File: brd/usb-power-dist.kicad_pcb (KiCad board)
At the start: 2 copper layers, 50 x 50 mm, 40 parts, among them J1 POWER IN, J2 USB_A, J3 USB_A, J4 CASC IN, J5 CASC OUT, U1 TPS2552D, U2 TPS2552D, U3 TPS2513

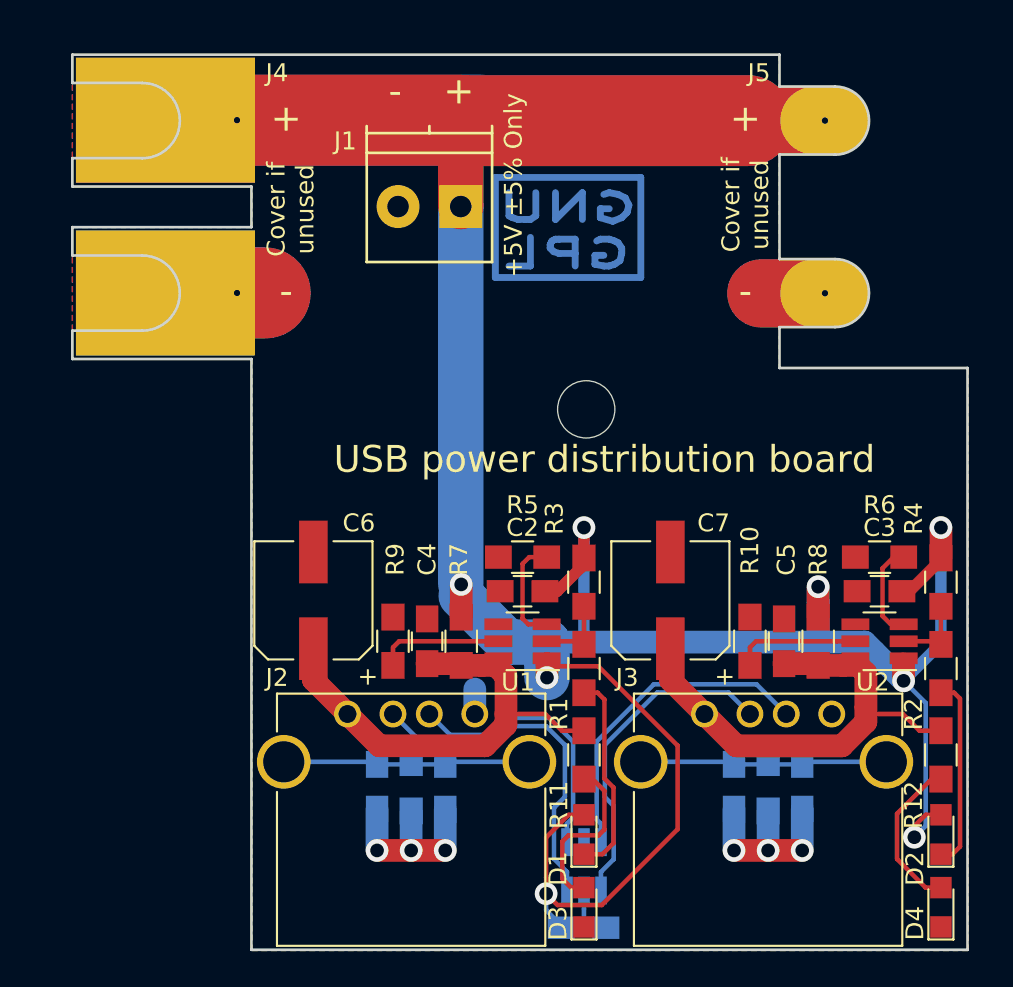
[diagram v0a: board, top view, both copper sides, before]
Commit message: recolocados componentes por fallo en asignacion de pines en TPS2552, modificada posicion de serigrafias, añadida serigrafia de version y tabla de corriente, cambiado footprint de conector de entrada y alargados conectores de borde de placa de cascada machos
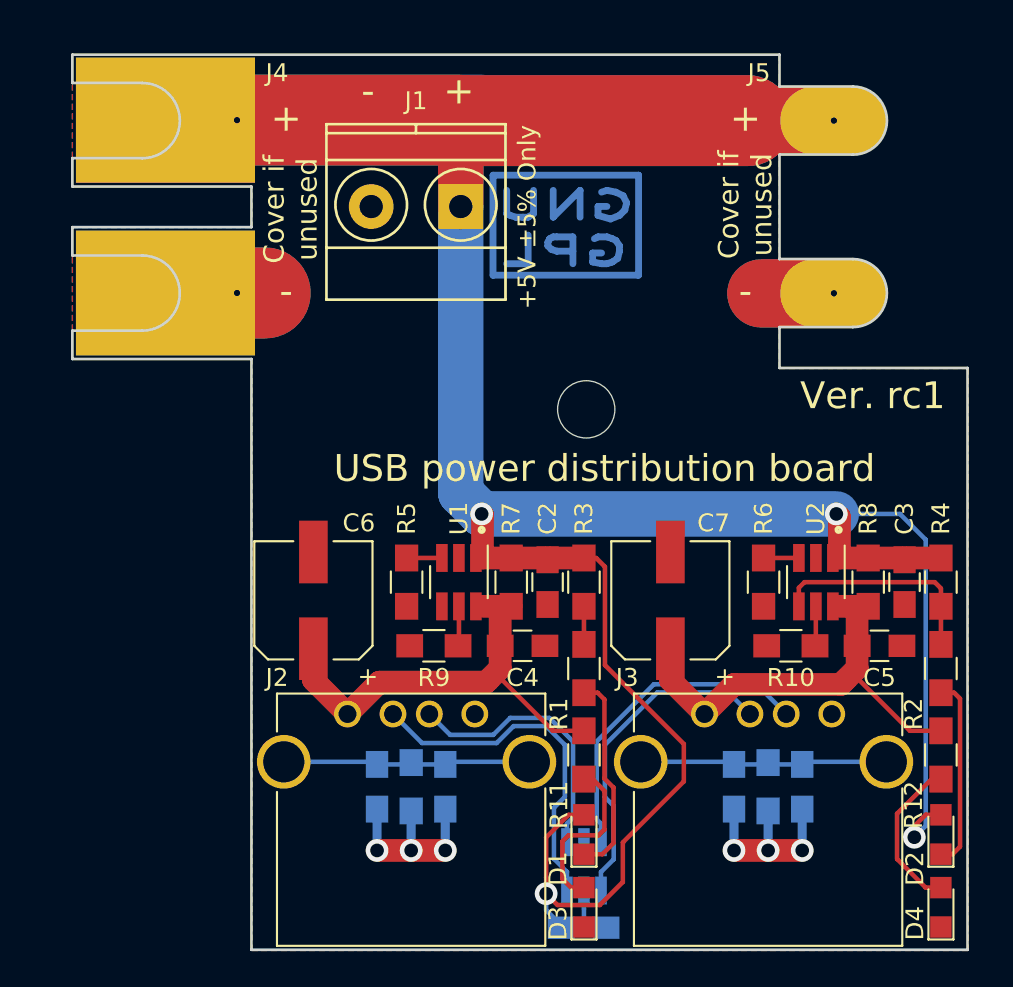
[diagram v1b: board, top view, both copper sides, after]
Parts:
- J1: footprint Terminal_Blocks:TerminalBlock_Pheonix_PT-3.5mm_2pol -> Terminal_Blocks:TerminalBlock_Pheonix_MKDS1.5-2pol
- moved R5 6.63 mm to (141.6, 110.5), turned to 270 degrees
- moved R6 6.63 mm to (161.5, 110.5), turned to 270 degrees
- moved C4 5.34 mm to (148.1, 114.0), turned to 0 degrees
- moved C5 5.34 mm to (168.0, 114.0), turned to 0 degrees
- moved U1 4.85 mm to (144.5, 110.5), turned to 270 degrees
- moved U2 4.85 mm to (164.5, 110.5), turned to 270 degrees
- moved R7 4.33 mm to (147.4, 110.5)
- moved R8 4.33 mm to (167.4, 110.5)
- moved R10 2.30 mm to (163.1, 114.0), turned to 180 degrees
- moved R9 2.30 mm to (143.1, 114.0), turned to 180 degrees
- moved C2 1.49 mm to (149.5, 110.5), turned to 270 degrees
- moved C3 1.49 mm to (169.4, 110.5), turned to 270 degrees
- moved REF** 0.18 mm to (150.5, 90.8)
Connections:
- U1 pad 2: Net-(R1-Pad1) -> GND
- U1 pad 4: GND -> Net-(R1-Pad1)
- U2 pad 2: Net-(R2-Pad1) -> GND
- U2 pad 4: GND -> Net-(R2-Pad1)
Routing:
- net +5V: track 205.9 -> 193.4 mm, vias 8 -> 4
- net Net-(R2-Pad1): track 4.28 -> 12.6 mm
- net Net-(R9-Pad1): track 7.04 -> 2.23 mm
- net Net-(R10-Pad1): track 7.04 -> 2.23 mm
- net Net-(R5-Pad1): track 6.05 -> 1.97 mm
- net Net-(R6-Pad1): track 5.48 -> 1.97 mm
- net Net-(C5-Pad1): track 28.1 -> 25.7 mm
- net Net-(R1-Pad1): track 4.28 -> 2.13 mm
- net Net-(C4-Pad1): track 27.8 -> 25.7 mm
- net GND: track 32.9 -> 33.5 mm
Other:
- outline, holes or cut-outs redrawn
- board text added: "Current R9/R10 100mA 226k 500mA 52k3 900mA 28k7 1500mA 16k9 No lim See doc"
- board text added: "Ver. rc1"
- board text removed: "[X] Comprobar footprints de conectores [X] Ubicación de montaje [X] Verificar forma de placa [X] Trazado completo [X] Colocar serigrafia [X] Añadir textos, polaridad y logos"

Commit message: corregido fallo ausencia de pista pin ¬FAULT
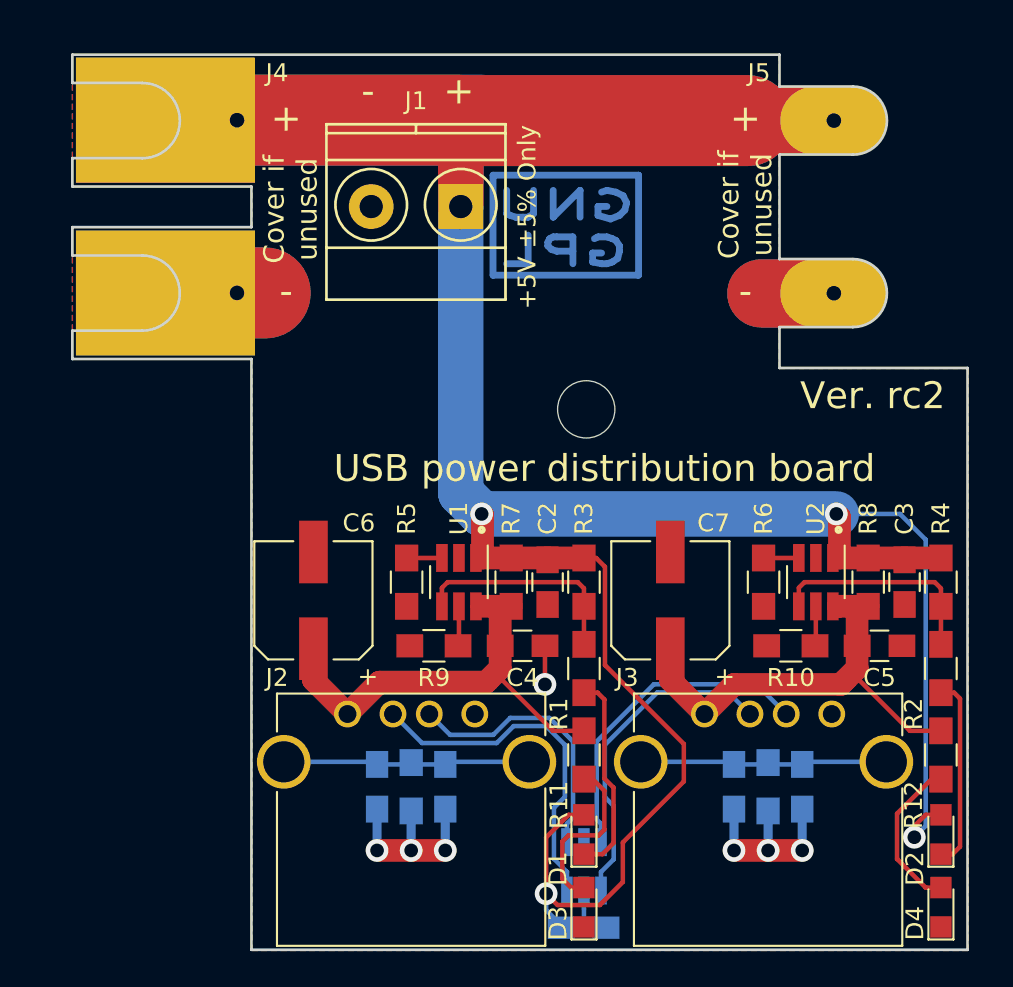
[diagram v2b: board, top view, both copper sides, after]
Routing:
- net Net-(R1-Pad1): track 2.13 -> 12.4 mm
- net GND: track 33.5 -> 36.0 mm, vias 6 -> 7
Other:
- board text added: "Ver. rc2"
- board text removed: "Ver. rc1"
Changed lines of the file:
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@@
   (general
     (links 74)
-    (no_connects 6)
-    (area 122.860999 80.950999 173.011001 131.101001)
+    (no_connects 5)
+    (area 101.330001 62.705 205.957143 139.733001)
     (thickness 1.6)
     (drawings 77)
-    (tracks 196)
+    (tracks 203)
     (zones 0)
     (modules 40)
@@
     (mod_text_size 1 1)
     (mod_text_width 0.15)
-    (pad_size 3.8 6)
-    (pad_drill 0.35)
+    (pad_size 7 10)
+    (pad_drill 0.8128)
     (pad_to_mask_clearance 0.2)
     (aux_axis_origin 0 0)
@@
     (add_net "Net-(C5-Pad1)")
   )
-  (module Capacitors_SMD:C_0805_HandSoldering (layer F.Cu)
-    (at 149.479 110.49 270)
-    (descr "Capacitor SMD 0805, hand soldering")
-    (tags "capacitor 0805")
-    (attr smd)
-    (fp_text reference C2 (at -3.556 0 270) (layer F.SilkS)
-      (effects (font (size 1 1) (thickness 0.15)))
-    )
-    (fp_text value 100nF (at 0 3.556 270) (layer F.Fab) hide
-      (effects (font (size 1 1) (thickness 0.15)))
-    )
-    (fp_text user %R (at 0 3.556 270) (layer F.Fab) hide
-      (effects (font (size 1 1) (thickness 0.15)))
-    )
-    (fp_line (start -1 0.62) (end -1 -0.62) (layer F.Fab) (width 0.1))
-    (fp_line (start 1 0.62) (end -1 0.62) (layer F.Fab) (width 0.1))
-    (fp_line (start 1 -0.62) (end 1 0.62) (layer F.Fab) (width 0.1))
-    (fp_line (start -1 -0.62) (end 1 -0.62) (layer F.Fab) (width 0.1))
-    (fp_line (start 0.5 -0.85) (end -0.5 -0.85) (layer F.SilkS) (width 0.12))
-    (fp_line (start -0.5 0.85) (end 0.5 0.85) (layer F.SilkS) (width 0.12))
-    (fp_line (start -2.25 -0.88) (end 2.25 -0.88) (layer F.CrtYd) (width 0.05))
-    (fp_line (start -2.25 -0.88) (end -2.25 0.87) (layer F.CrtYd) (width 0.05))
-    (fp_line (start 2.25 0.87) (end 2.25 -0.88) (layer F.CrtYd) (width 0.05))
-    (fp_line (start 2.25 0.87) (end -2.25 0.87) (layer F.CrtYd) (width 0.05))
-    (pad 1 smd rect (at -1.25 0 270) (size 1.5 1.25) (layers F.Cu F.Paste F.Mask)
-      (net 1 +5V))
-    (pad 2 smd rect (at 1.25 0 270) (size 1.5 1.25) (layers F.Cu F.Paste F.Mask)
-      (net 2 GND))
-    (model Capacitors_SMD.3dshapes/C_0805.wrl
-      (at (xyz 0 0 0))
-      (scale (xyz 1 1 1))
-      (rotate (xyz 0 0 0))
-    )
-  )
   (module TO_SOT_Packages_SMD:SOT-23-6_Handsoldering (layer F.Cu)
     (at 144.526 110.49 270)
@@
       (net 19 "Net-(R9-Pad1)"))
     (model ${KISYS3DMOD}/TO_SOT_Packages_SMD.3dshapes/SOT-23-6.wrl
+      (at (xyz 0 0 0))
+      (scale (xyz 1 1 1))
+      (rotate (xyz 0 0 0))
+    )
+  )
+  (module Capacitors_SMD:C_0805_HandSoldering (layer F.Cu)
+    (at 149.479 110.49 270)
+    (descr "Capacitor SMD 0805, hand soldering")
+    (tags "capacitor 0805")
+    (attr smd)
+    (fp_text reference C2 (at -3.556 0 270) (layer F.SilkS)
+      (effects (font (size 1 1) (thickness 0.15)))
+    )
+    (fp_text value 100nF (at 0 3.556 270) (layer F.Fab) hide
+      (effects (font (size 1 1) (thickness 0.15)))
+    )
+    (fp_text user %R (at 0 3.556 270) (layer F.Fab) hide
+      (effects (font (size 1 1) (thickness 0.15)))
+    )
+    (fp_line (start -1 0.62) (end -1 -0.62) (layer F.Fab) (width 0.1))
+    (fp_line (start 1 0.62) (end -1 0.62) (layer F.Fab) (width 0.1))
+    (fp_line (start 1 -0.62) (end 1 0.62) (layer F.Fab) (width 0.1))
+    (fp_line (start -1 -0.62) (end 1 -0.62) (layer F.Fab) (width 0.1))
+    (fp_line (start 0.5 -0.85) (end -0.5 -0.85) (layer F.SilkS) (width 0.12))
+    (fp_line (start -0.5 0.85) (end 0.5 0.85) (layer F.SilkS) (width 0.12))
+    (fp_line (start -2.25 -0.88) (end 2.25 -0.88) (layer F.CrtYd) (width 0.05))
+    (fp_line (start -2.25 -0.88) (end -2.25 0.87) (layer F.CrtYd) (width 0.05))
+    (fp_line (start 2.25 0.87) (end 2.25 -0.88) (layer F.CrtYd) (width 0.05))
+    (fp_line (start 2.25 0.87) (end -2.25 0.87) (layer F.CrtYd) (width 0.05))
+    (pad 1 smd rect (at -1.25 0 270) (size 1.5 1.25) (layers F.Cu F.Paste F.Mask)
+      (net 1 +5V))
+    (pad 2 smd rect (at 1.25 0 270) (size 1.5 1.25) (layers F.Cu F.Paste F.Mask)
+      (net 2 GND))
+    (model Capacitors_SMD.3dshapes/C_0805.wrl
       (at (xyz 0 0 0))
       (scale (xyz 1 1 1))
@@
     (fp_line (start -2.6162 -4.1148) (end -2.1336 -5.1816) (layer Cmts.User) (width 0.381))
     (fp_line (start -2.1336 -5.1816) (end -2.1336 -3.6322) (layer Cmts.User) (width 0.381))
-    (pad 1 thru_hole rect (at 0.508 0.127 270) (size 7 10) (drill 0.35 (offset 0 4)) (layers *.Cu *.Mask)
+    (pad 1 thru_hole rect (at 0.508 0.127 270) (size 7 10) (drill 0.8128 (offset 0 4)) (layers *.Cu *.Mask)
       (net 1 +5V))
-    (pad 2 thru_hole rect (at 10.16 0.127 270) (size 7 10) (drill 0.35 (offset 0 4)) (layers *.Cu *.Mask)
+    (pad 2 thru_hole rect (at 10.16 0.127 270) (size 7 10) (drill 0.8128 (offset 0 4)) (layers *.Cu *.Mask)
       (net 2 GND))
   )
@@
     (fp_line (start -2.6162 -4.1148) (end -2.1336 -5.1816) (layer Cmts.User) (width 0.381))
     (fp_line (start -2.1336 -5.1816) (end -2.1336 -3.6322) (layer Cmts.User) (width 0.381))
-    (pad 1 thru_hole oval (at 0 1.532 270) (size 3.8 6) (drill 0.35) (layers *.Cu *.Mask)
+    (pad 1 thru_hole oval (at 0 1.532 270) (size 3.8 6) (drill 0.8128) (layers *.Cu *.Mask)
       (net 1 +5V))
-    (pad 2 thru_hole oval (at 9.643 1.532 270) (size 3.8 6) (drill 0.35) (layers *.Cu *.Mask)
+    (pad 2 thru_hole oval (at 9.643 1.532 270) (size 3.8 6) (drill 0.8128) (layers *.Cu *.Mask)
       (net 2 GND))
   )
@@
     )
   )
-  (gr_text "Ver. rc1" (at 167.64 100.076) (layer F.SilkS)
+  (gr_text "Ver. rc2" (at 167.64 100.076) (layer F.SilkS)
     (effects (font (size 1.5 1.5) (thickness 0.15)))
   )
@@
   (segment (start 151.245 129.794) (end 151.511 129.528) (width 0.254) (layer B.Cu) (net 1))
   (segment (start 151.511 129.528) (end 151.511 128.749) (width 0.254) (layer B.Cu) (net 1))
+  (segment (start 149.332 116.200199) (end 149.330626 116.201573) (width 0.254) (layer F.Cu) (net 2))
+  (segment (start 149.454199 116.078) (end 149.330626 116.201573) (width 0.254) (layer B.Cu) (net 2))
+  (segment (start 149.332 114.046) (end 149.332 116.200199) (width 0.254) (layer F.Cu) (net 2))
+  (segment (start 149.606 116.078) (end 149.454199 116.078) (width 0.254) (layer B.Cu) (net 2))
+  (via (at 149.330626 116.201573) (size 1.27) (drill 0.762) (layers F.Cu B.Cu) (net 2))
   (segment (start 132.1308 94.3356) (end 133.7056 94.3356) (width 5.08) (layer F.Cu) (net 2))
   (segment (start 132.1308 94.3356) (end 133.7056 94.3356) (width 5.08) (layer B.Cu) (net 2))
@@
   (segment (start 139.954 123.17) (end 139.954 125.476) (width 0.508) (layer B.Cu) (net 2))
   (via (at 139.954 125.476) (size 1.27) (drill 0.762) (layers F.Cu B.Cu) (net 2))
+  (segment (start 147.447 111.84) (end 145.796165 111.84) (width 1.27) (layer F.Cu) (net 3))
   (segment (start 146.05 116.078) (end 146.177 115.951) (width 1.27) (layer F.Cu) (net 3))
   (segment (start 146.177 115.951) (end 146.832 115.296) (width 1.27) (layer F.Cu) (net 3))
@@
   (segment (start 140.081 116.078) (end 146.05 116.078) (width 1.27) (layer F.Cu) (net 3))
   (segment (start 146.832 115.296) (end 146.832 114.046) (width 1.27) (layer F.Cu) (net 3))
-  (segment (start 147.447 111.84) (end 146.558 111.84) (width 1.27) (layer F.Cu) (net 3))
-  (segment (start 146.558 111.84) (end 145.843 111.84) (width 1.27) (layer F.Cu) (net 3))
   (segment (start 146.832 114.046) (end 146.832 112.114) (width 1.27) (layer F.Cu) (net 3))
-  (segment (start 146.832 112.114) (end 146.558 111.84) (width 1.27) (layer F.Cu) (net 3))
   (segment (start 151.511 118.792) (end 149.78 118.792) (width 0.254) (layer F.Cu) (net 3))
   (segment (start 136.398 114.206) (end 136.398 115.951) (width 1.27) (layer F.Cu) (net 3))
   (segment (start 136.398 115.951) (end 138.303 117.856) (width 1.27) (layer F.Cu) (net 3))
+  (segment (start 167.386 111.84) (end 165.732062 111.84) (width 1.27) (layer F.Cu) (net 4))
+  (segment (start 165.732062 111.84) (end 165.731194 111.839132) (width 1.27) (layer F.Cu) (net 4))
   (segment (start 165.862 116.205) (end 166.116 115.951) (width 1.27) (layer F.Cu) (net 4))
   (segment (start 166.116 115.951) (end 166.771 115.296) (width 1.27) (layer F.Cu) (net 4))
@@
   (segment (start 159.893 116.205) (end 165.862 116.205) (width 1.27) (layer F.Cu) (net 4))
   (segment (start 166.771 115.296) (end 166.771 114.046) (width 1.27) (layer F.Cu) (net 4))
-  (segment (start 167.386 111.84) (end 166.497 111.84) (width 1.27) (layer F.Cu) (net 4))
-  (segment (start 166.497 111.84) (end 165.782 111.84) (width 1.27) (layer F.Cu) (net 4))
   (segment (start 166.771 114.046) (end 166.771 112.114) (width 1.27) (layer F.Cu) (net 4))
-  (segment (start 166.771 112.114) (end 166.497 111.84) (width 1.27) (layer F.Cu) (net 4))
   (segment (start 156.337 114.206) (end 156.337 115.951) (width 1.27) (layer F.Cu) (net 4))
   (segment (start 156.337 115.951) (end 158.242 117.856) (width 1.27) (layer F.Cu) (net 4))
@@
   (segment (start 153.173018 125.968982) (end 152.461 126.681) (width 0.254) (layer B.Cu) (net 14))
   (segment (start 152.461 126.681) (end 152.461 127.715) (width 0.254) (layer B.Cu) (net 14))
+  (segment (start 143.576 111.84) (end 143.576 110.809571) (width 0.254) (layer F.Cu) (net 15))
+  (segment (start 143.576 110.809571) (end 143.895571 110.49) (width 0.254) (layer F.Cu) (net 15))
+  (segment (start 143.895571 110.49) (end 151.164173 110.49) (width 0.254) (layer F.Cu) (net 15))
+  (segment (start 151.164173 110.49) (end 151.511 110.836827) (width 0.254) (layer F.Cu) (net 15))
+  (segment (start 151.511 110.836827) (end 151.511 111.84) (width 0.254) (layer F.Cu) (net 15))
   (segment (start 151.511 111.84) (end 151.511 113.966) (width 0.254) (layer F.Cu) (net 15))
   (segment (start 163.515 111.84) (end 163.515 110.806) (width 0.254) (layer F.Cu) (net 16))

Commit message: añadido plateado de contactos mediante vias, añadido marcado de PCB y verificacion general
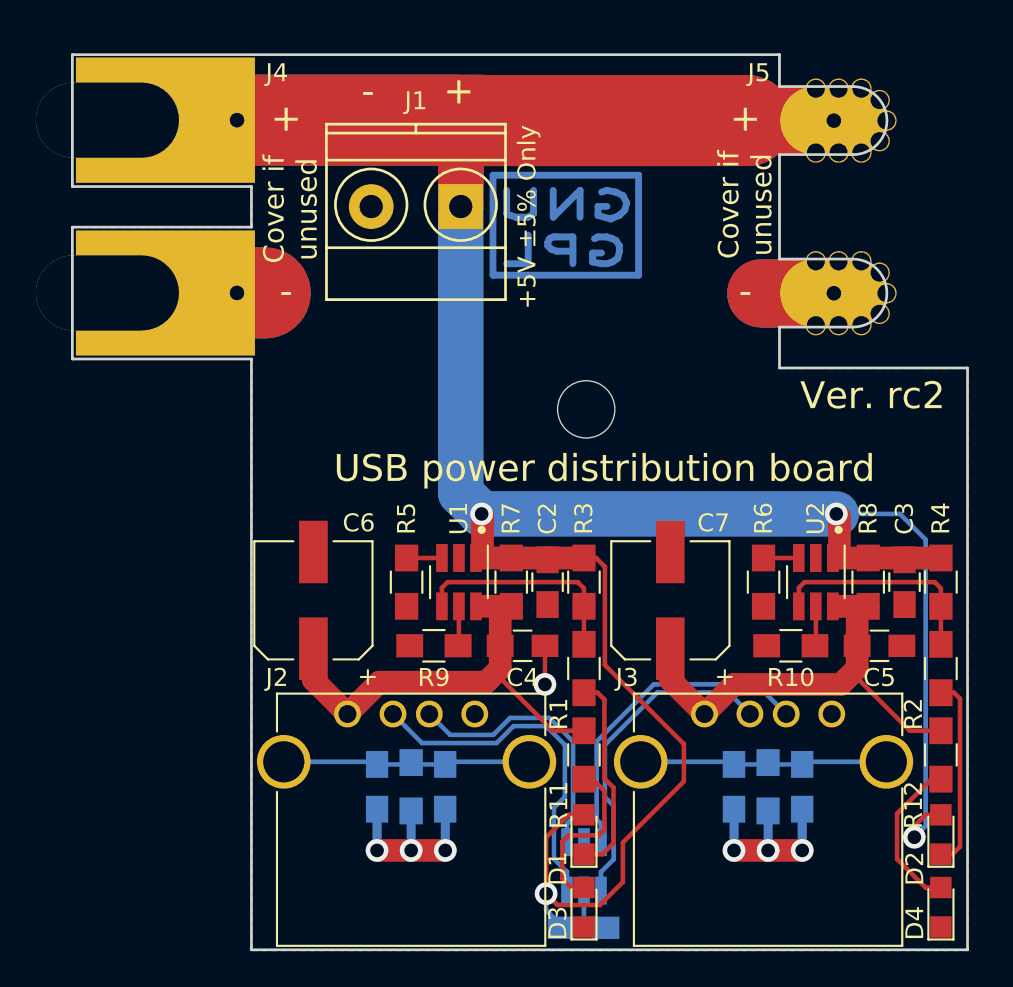
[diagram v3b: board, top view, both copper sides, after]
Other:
- outline, holes or cut-outs redrawn
- board text added: "k099C8134/3-d0917"
